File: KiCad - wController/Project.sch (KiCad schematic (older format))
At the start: 11 parts, among them IC1 ATMEGA328-P, P1 CONN_02X03, P2 CONN_01X02, SW4 SW_PUSH, U1 BlueSmirf, Y1 Crystal

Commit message: Started with the PCB
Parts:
- removed P2: CONN_01X02, Pin_Headers:Pin_Header_Straight_1x02, symbol CONN_01X02
- P1: footprint Pin_Headers:Pin_Header_Straight_2x03 -> Pin_Headers:Pin_Header_Angled_2x03
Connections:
- net IR/5V: now also P1.2 (P2)
- no-connect marks 10 -> 0
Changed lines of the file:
@@
 $Descr A4 11693 8268
 encoding utf-8
-Sheet 1 5
+Sheet 1 6
 Title ""
 Date ""
@@
 $EndComp
 $Comp
-L GND #PWR1
+L GND #PWR01
 U 1 1 5715DC43
 P 1500 3800
-F 0 "#PWR1" H 1500 3550 50  0001 C CNN
+F 0 "#PWR01" H 1500 3550 50  0001 C CNN
 F 1 "GND" H 1500 3650 50  0000 C CNN
 F 2 "" H 1500 3800 50  0000 C CNN
@@
 	8850 4900 8800 4900
 $Comp
-L GND #PWR7
+L GND #PWR02
 U 1 1 57165880
 P 8800 4900
-F 0 "#PWR7" H 8800 4650 50  0001 C CNN
+F 0 "#PWR02" H 8800 4650 50  0001 C CNN
 F 1 "GND" H 8800 4750 50  0000 C CNN
 F 2 "" H 8800 4900 50  0000 C CNN
@@
 	4150 2100 3500 2100
 $Comp
-L GND #PWR4
+L GND #PWR03
 U 1 1 5716EE89
 P 4450 1800
-F 0 "#PWR4" H 4450 1550 50  0001 C CNN
+F 0 "#PWR03" H 4450 1550 50  0001 C CNN
 F 1 "GND" H 4450 1650 50  0000 C CNN
 F 2 "" H 4450 1800 50  0000 C CNN
@@
 Wire Wire Line
 	4200 2600 3500 2600
+$Sheet
+S 1750 4600 1100 650
+U 5717B094
+F0 "Controller" 60
+F1 "Controller.sch" 60
+$EndSheet
 Wire Wire Line
 	8200 5400 9500 5400
@@
 F 0 "P1" H 3950 1850 50  0000 C CNN
 F 1 "CONN_02X03" H 3950 1450 50  0000 C CNN
-F 2 "Pin_Headers:Pin_Header_Straight_2x03" H 3950 450 50  0001 C CNN
+F 2 "Pin_Headers:Pin_Header_Angled_2x03" H 3950 450 50  0001 C CNN
 F 3 "" H 3950 450 50  0000 C CNN
 	1    3950 1650
@@
 	3700 1750 3500 1750
 Wire Wire Line
+	4550 1000 4550 1550
+Wire Wire Line
+	4550 1550 4200 1550
+Connection ~ 4550 1000
+Wire Wire Line
 	4200 1750 4300 1750
 Wire Wire Line
@@
 	4300 2700 3500 2700
 $Comp
-L GND #PWR3
+L GND #PWR04
 U 1 1 5733AA01
 P 4250 1650
-F 0 "#PWR3" H 4250 1400 50  0001 C CNN
+F 0 "#PWR04" H 4250 1400 50  0001 C CNN
 F 1 "GND" H 4250 1500 50  0000 C CNN
 F 2 "" H 4250 1650 50  0000 C CNN
@@
 $EndComp
 $Comp
-L GND #PWR5
+L GND #PWR05
 U 1 1 5733D1EA
 P 6650 2300
-F 0 "#PWR5" H 6650 2050 50  0001 C CNN
+F 0 "#PWR05" H 6650 2050 50  0001 C CNN
 F 1 "GND" H 6650 2150 50  0000 C CNN
 F 2 "" H 6650 2300 50  0000 C CNN
@@
 $EndComp
 $Comp
-L GND #PWR6
+L GND #PWR06
 U 1 1 5733D278
 P 6850 2650
-F 0 "#PWR6" H 6850 2400 50  0001 C CNN
+F 0 "#PWR06" H 6850 2400 50  0001 C CNN
 F 1 "GND" H 6850 2500 50  0000 C CNN
 F 2 "" H 6850 2650 50  0000 C CNN
@@
 $EndComp
 $Comp
-L GND #PWR2
+L GND #PWR07
 U 1 1 5734269F
 P 3650 4700
-F 0 "#PWR2" H 3650 4450 50  0001 C CNN
+F 0 "#PWR07" H 3650 4450 50  0001 C CNN
 F 1 "GND" H 3650 4550 50  0000 C CNN
 F 2 "" H 3650 4700 50  0000 C CNN
@@
 Wire Wire Line
 	5200 3500 5750 3500
-$Comp
-L CONN_01X02 P2
-U 1 1 5734FE54
-P 8350 2400
-F 0 "P2" H 8350 2550 50  0000 C CNN
-F 1 "CONN_01X02" V 8450 2400 50  0000 C CNN
-F 2 "Pin_Headers:Pin_Header_Straight_1x02" H 8350 2400 50  0000 C CNN
-F 3 "" H 8350 2400 50  0000 C CNN
-	1    8350 2400
-	1    0    0    -1
-$EndComp
-Wire Wire Line
-	8150 2350 7450 2350
-Wire Wire Line
-	7450 2350 7450 2850
-Connection ~ 7450 2850
-Wire Wire Line
-	7550 2450 7550 2950
-Wire Wire Line
-	7550 2450 8150 2450
-Connection ~ 7550 2950
-NoConn ~ 4200 1550
-NoConn ~ 8550 4100
-NoConn ~ 9050 4100
-NoConn ~ 3500 1350
-NoConn ~ 3500 1450
-NoConn ~ 3500 2200
-NoConn ~ 3500 2300
-NoConn ~ 3500 3250
-NoConn ~ 3500 3550
-NoConn ~ 1600 1550
 $EndSCHEMATC

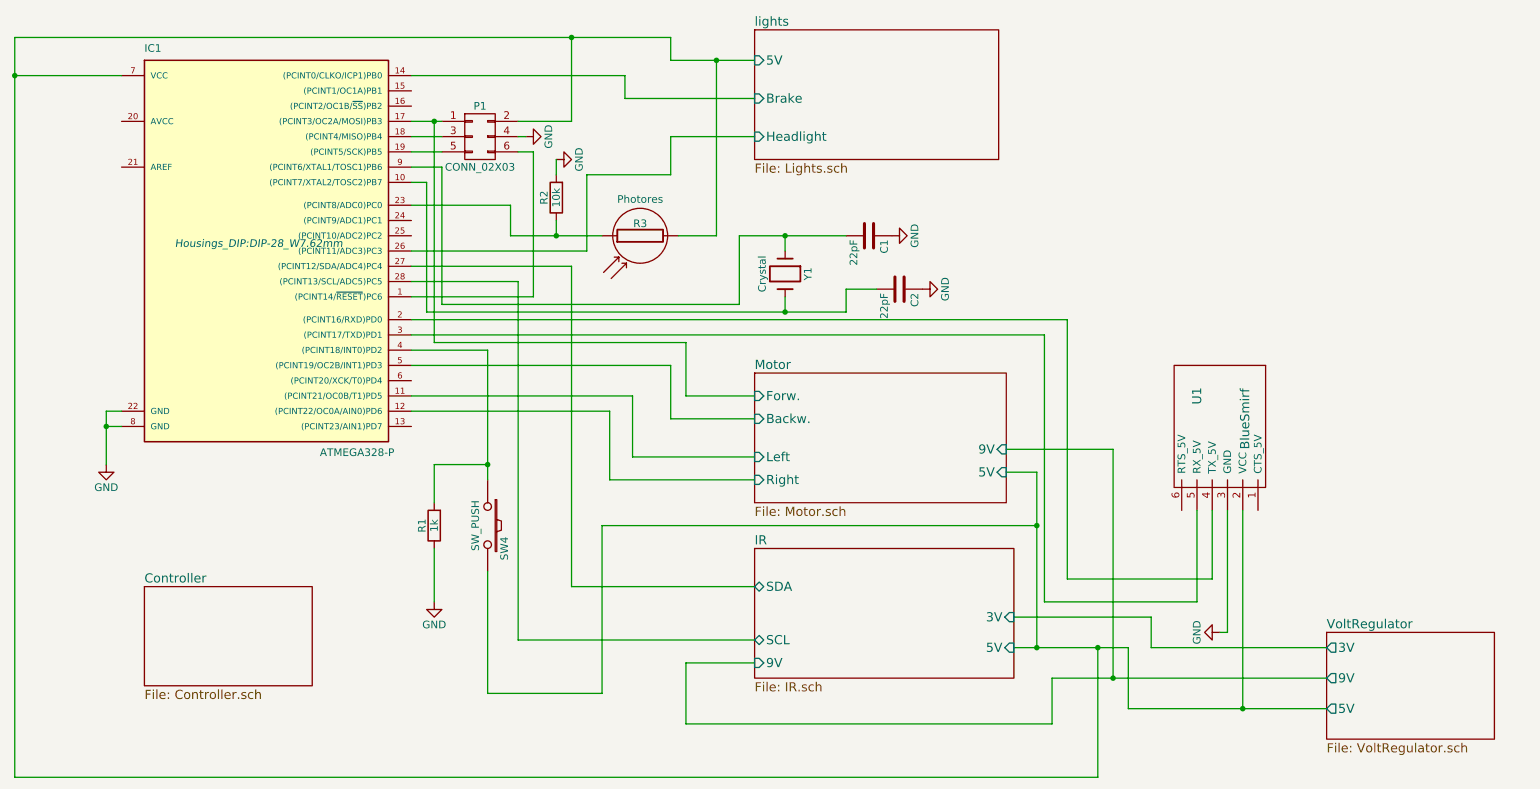
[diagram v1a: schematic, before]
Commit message: Added code and created PCB for controller
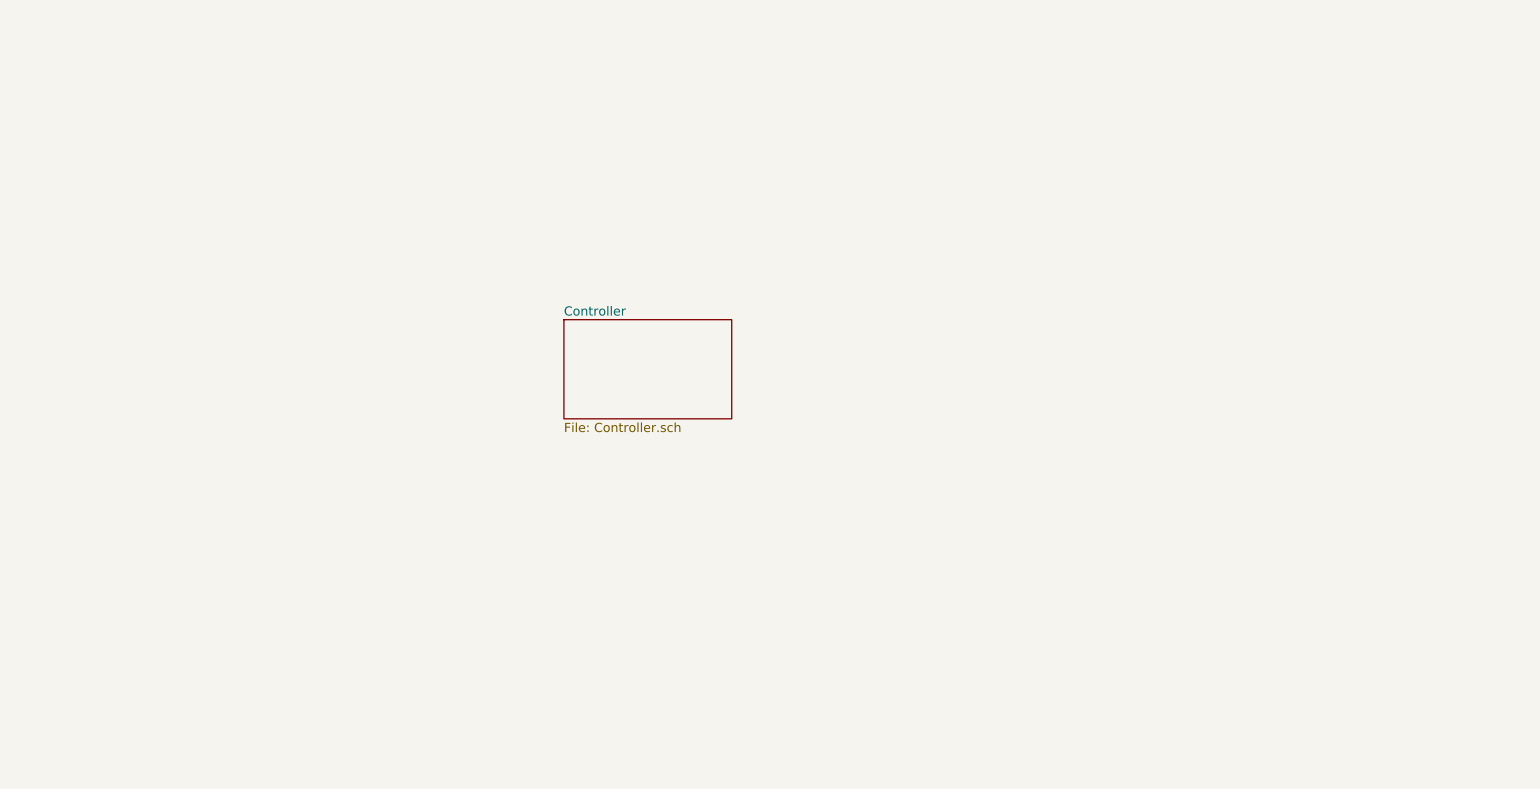
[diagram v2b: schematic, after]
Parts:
- removed C1, C2: 22pF, Capacitors_ThroughHole:C_Disc_D3_P2.5, symbol C
- removed IC1: ATMEGA328-P, Housings_DIP:DIP-28_W7.62mm, symbol ATMEGA328-P
- removed P1: CONN_02X03, Pin_Headers:Pin_Header_Angled_2x03, symbol CONN_02X03
- removed R1: 1k, Resistors_ThroughHole:Resistor_Vertical_RM5mm, symbol R
- removed R2: 10k, Resistors_ThroughHole:Resistor_Vertical_RM5mm, symbol R
- removed R3: Photores, Wire_Connections_Bridges:WireConnection_1.50mmDrill, symbol Photores
- removed SW4: SW_PUSH, Wire_Connections_Bridges:WireConnection_1.50mmDrill, symbol SW_PUSH
- removed U1: BlueSmirf, Pin_Headers:Pin_Header_Straight_1x06, symbol BlueSmirf
- removed Y1: Crystal, Crystals:Crystal_HC52-U_Vertical, symbol Crystal
